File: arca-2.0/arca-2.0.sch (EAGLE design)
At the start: 192 parts, among them IC1 MCP6N11R, IC2 MCP6N11R, IC3 MCP6N11R, IC4 MCP6N11R, IC5 LM324D, IC6 LM324D, SW1 1101M2S3CQE2, SW2 1101M2S3CQE2, T1 FQP30N06L, T2 FQP30N06L, T3 FQP30N06L, T4 FQP30N06L, T5 FQP30N06L, T6 FQP30N06L, X1 2540-5

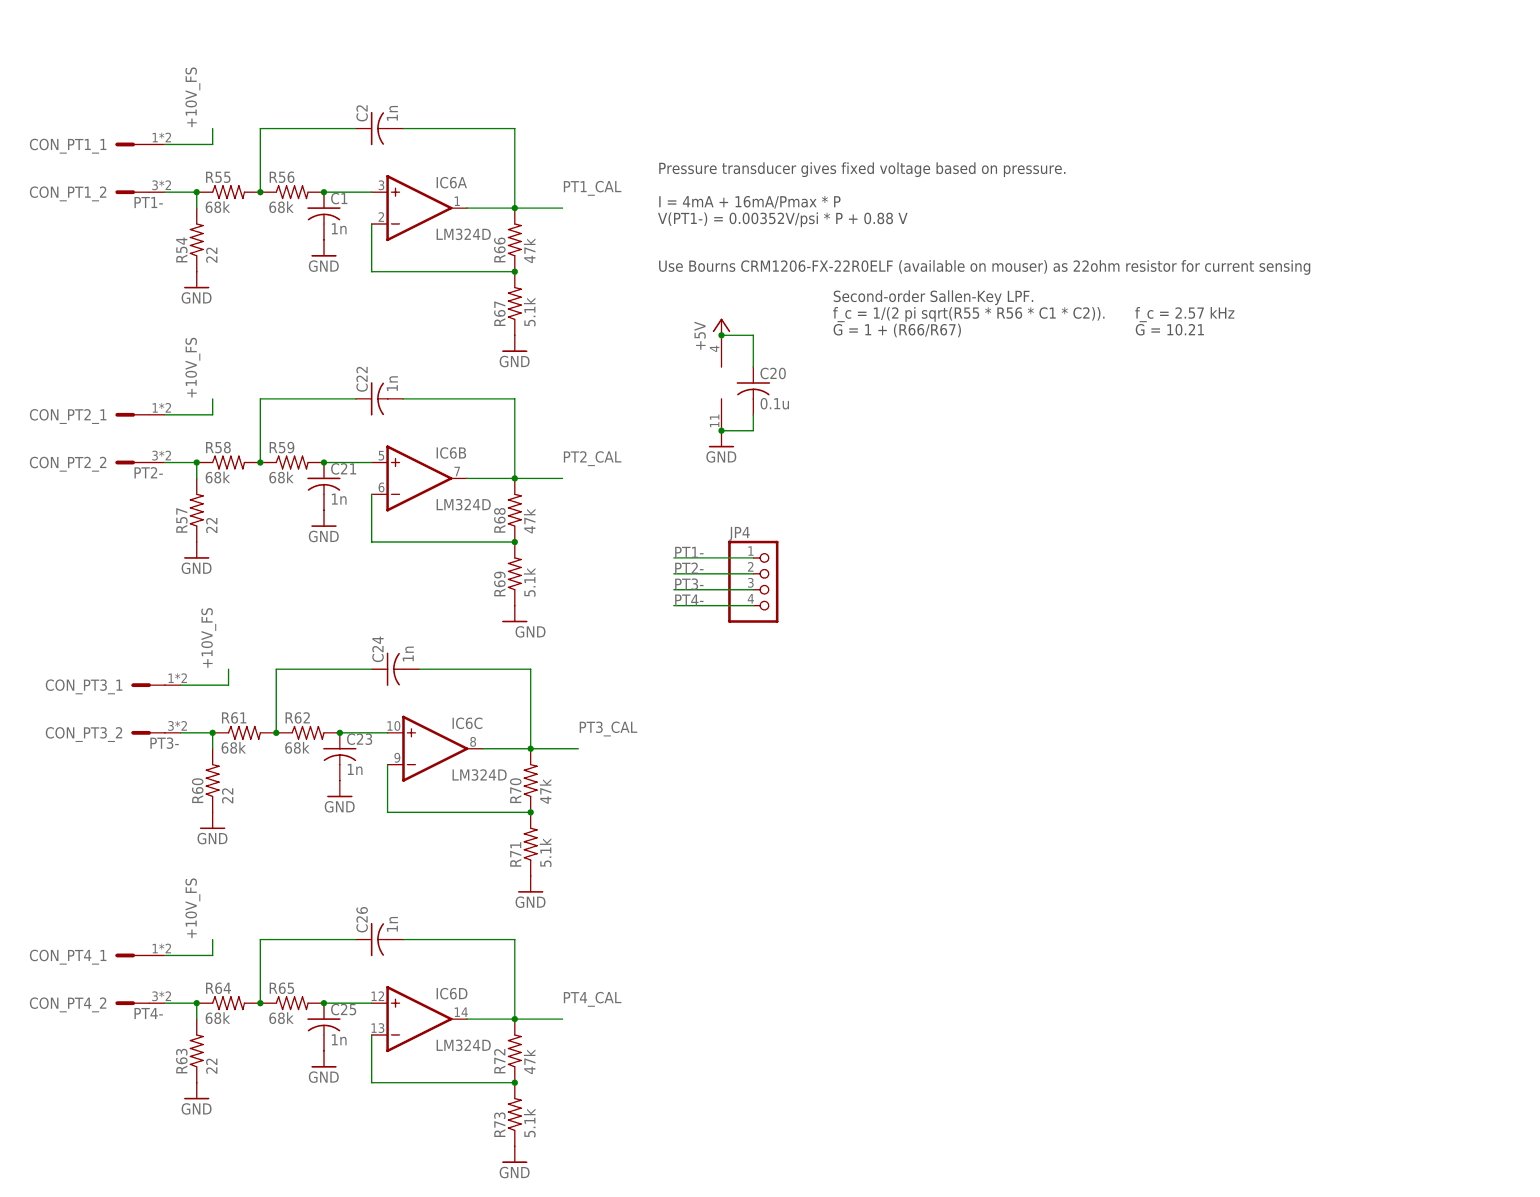
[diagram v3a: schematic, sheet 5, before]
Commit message: separate fuses for each external connection + LM324s on +10V
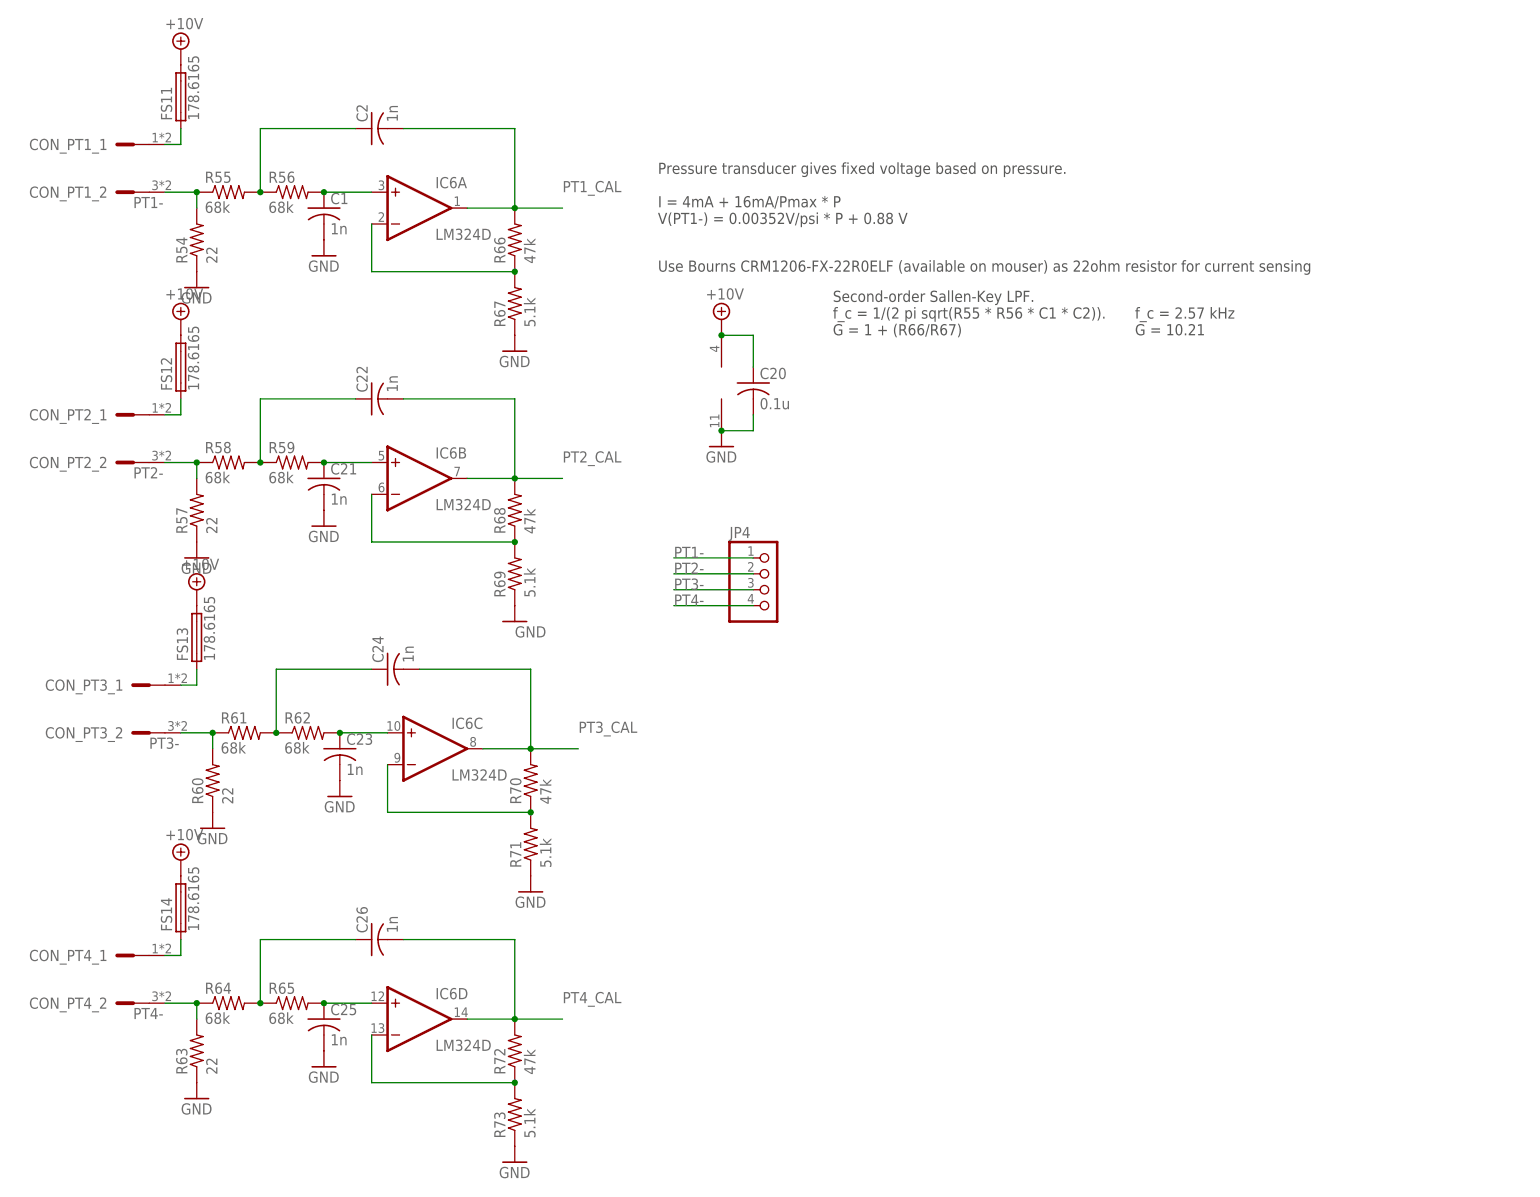
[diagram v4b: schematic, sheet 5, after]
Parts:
- added FS10, FS11, FS12, FS13, FS14, FS15, FS16, FS17, FS18, FS9: 178.6165, fuse-holder-littlefuse:178.6165
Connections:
- removed net +10V_FS: CON_PT1_1.SK, CON_PT2_1.SK, CON_PT3_1.SK, CON_PT4_1.SK, FS7.1
- removed net +5V_FS: CON_LC1_1.SK, CON_LC2_1.SK, CON_LC3_1.SK, CON_LC4_1.SK, CON_TC1_1.SK, CON_TC2_1.SK, CON_TC3_1.SK, CON_TC4_1.SK, FS8.1
- new net N$61: CON_LC1_1.SK, FS7.1
- new net N$62: CON_LC2_1.SK, FS8.1
- new net N$63: CON_LC3_1.SK, FS9.1
- new net N$64: CON_LC4_1.SK, FS10.1
- new net N$65: CON_PT1_1.SK, FS11.1
- new net N$66: CON_PT2_1.SK, FS12.1
- new net N$69: CON_PT3_1.SK, FS13.1
- new net N$70: CON_PT4_1.SK, FS14.1
- new net N$71: CON_TC1_1.SK, FS15.1
- new net N$72: CON_TC2_1.SK, FS16.1
- new net N$73: CON_TC3_1.SK, FS17.1
- new net N$74: CON_TC4_1.SK, FS18.1
- net +10V: now also C11.1, C20.1, FS11.2, FS12.2, FS13.2, FS14.2, IC5P.V+, IC6P.V+; no longer FS7.2
- net +5V: now also FS10.2, FS15.2, FS16.2, FS17.2, FS18.2, FS7.2, FS9.2; no longer C11.1, C20.1, IC5P.V+, IC6P.V+

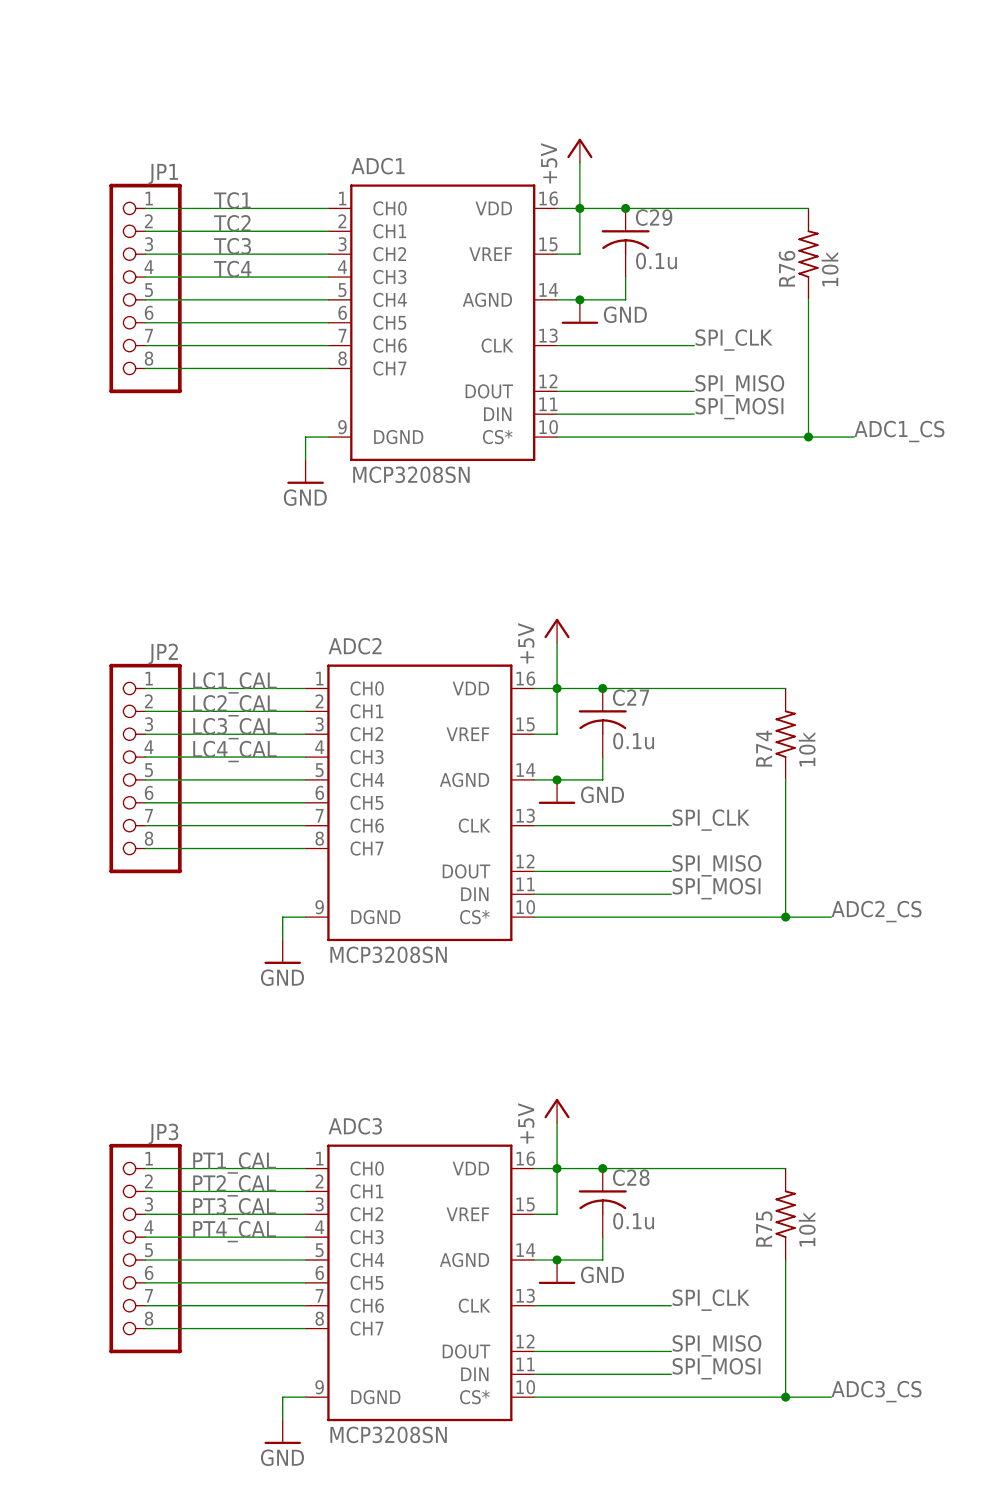
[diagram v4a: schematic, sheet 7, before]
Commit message: laying out extra breakers in board
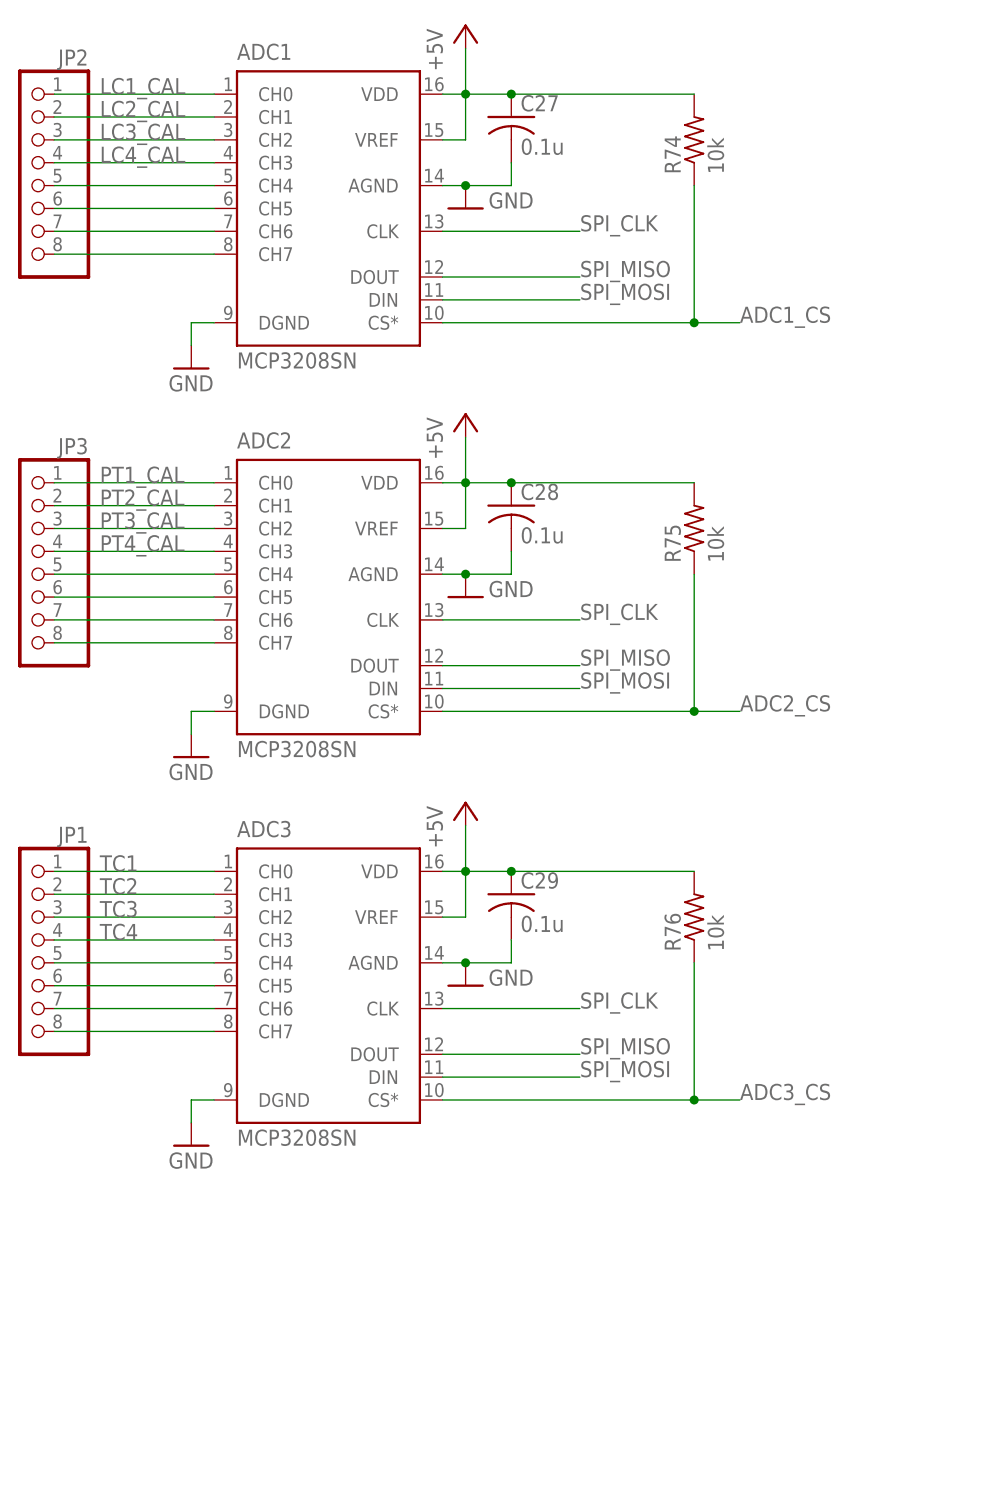
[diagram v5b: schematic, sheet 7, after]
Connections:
- net ADC1_CS: now also R74.1, X1-22.KL; no longer R76.1, X1-26.KL
- net ADC2_CS: now also R75.1; no longer R74.1
- net ADC3_CS: now also R76.1, X1-26.KL; no longer R75.1, X1-22.KL
- net LC1_CAL: now also ADC1.CH0; no longer ADC2.CH0
- net LC2_CAL: now also ADC1.CH1; no longer ADC2.CH1
- net LC3_CAL: now also ADC1.CH2; no longer ADC2.CH2
- net LC4_CAL: now also ADC1.CH3; no longer ADC2.CH3
- net N$49: now also ADC3.CH4; no longer ADC1.CH4
- net N$50: now also ADC3.CH5; no longer ADC1.CH5
- net N$51: now also ADC3.CH6; no longer ADC1.CH6
- net N$52: now also ADC3.CH7; no longer ADC1.CH7
- net N$53: now also ADC1.CH7; no longer ADC2.CH7
- net N$54: now also ADC1.CH6; no longer ADC2.CH6
- net N$55: now also ADC1.CH5; no longer ADC2.CH5
- net N$56: now also ADC1.CH4; no longer ADC2.CH4
- net N$57: now also ADC2.CH4; no longer ADC3.CH4
- net N$58: now also ADC2.CH5; no longer ADC3.CH5
- net N$59: now also ADC2.CH6; no longer ADC3.CH6
- net N$60: now also ADC2.CH7; no longer ADC3.CH7
- net PT1_CAL: now also ADC2.CH0; no longer ADC3.CH0
- net PT2_CAL: now also ADC2.CH1; no longer ADC3.CH1
- net PT3_CAL: now also ADC2.CH2; no longer ADC3.CH2
- net PT4_CAL: now also ADC2.CH3; no longer ADC3.CH3
- net TC1: now also ADC3.CH0; no longer ADC1.CH0
- net TC2: now also ADC3.CH1; no longer ADC1.CH1
- net TC3: now also ADC3.CH2; no longer ADC1.CH2
- net TC4: now also ADC3.CH3; no longer ADC1.CH3
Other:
- moved on the sheet: ADC1, ADC2, ADC3, C27, C28, C29, JP1, JP2, JP3, R74, R75, R76

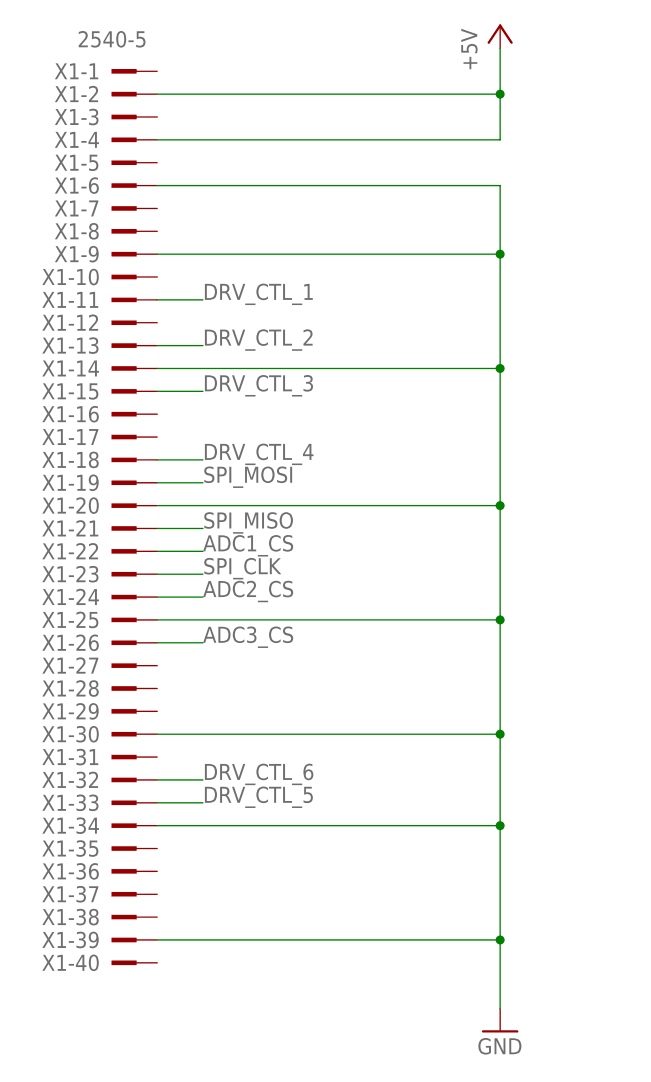
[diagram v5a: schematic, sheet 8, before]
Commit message: heartbeat light
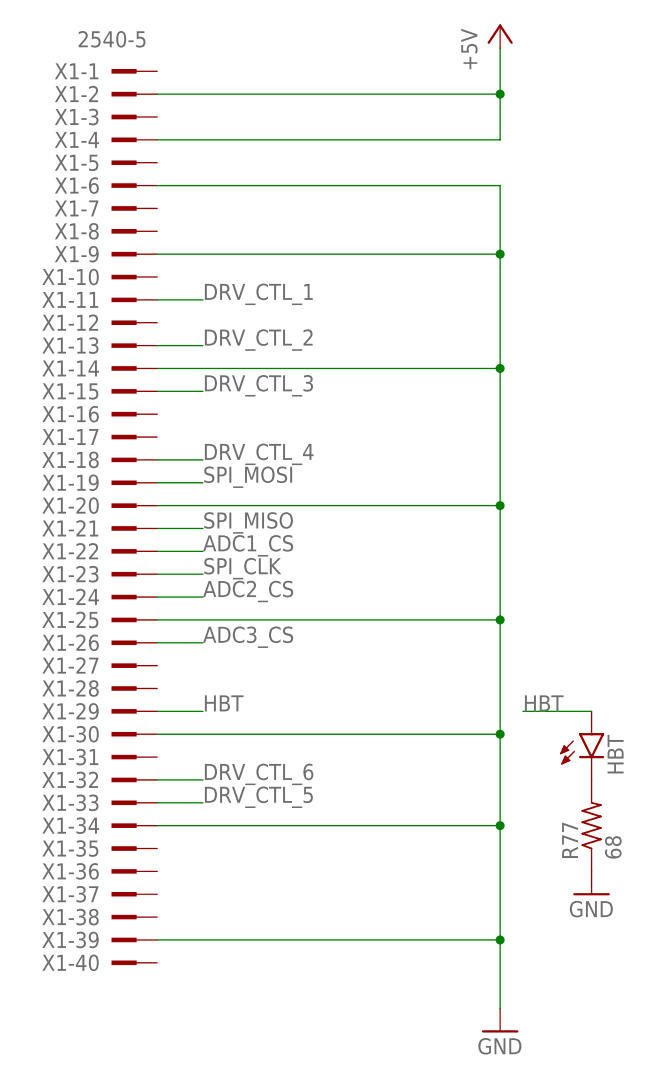
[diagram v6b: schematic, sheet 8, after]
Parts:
- added HBT: (no value), led:LEDCHIPLED_1206
- added R77: 68, rcl:R-US_R1206
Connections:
- new net HBT: HBT.A, X1-29.KL
- new net N$75: HBT.C, R77.2
- net GND: now also R77.1
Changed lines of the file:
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@@
 <part name="P+33" library="supply1" library_urn="urn:adsk.eagle:library:371" deviceset="+5V" device=""/>
 <part name="P+34" library="supply1" library_urn="urn:adsk.eagle:library:371" deviceset="+5V" device=""/>
+<part name="HBT" library="led" library_urn="urn:adsk.eagle:library:259" deviceset="LED" device="CHIPLED_1206" package3d_urn="urn:adsk.eagle:package:15823/2"/>
+<part name="R77" library="rcl" library_urn="urn:adsk.eagle:library:334" deviceset="R-US_" device="R1206" package3d_urn="urn:adsk.eagle:package:23540/2" value="68"/>
+<part name="GND69" library="supply1" library_urn="urn:adsk.eagle:library:371" deviceset="GND" device=""/>
 </parts>
 <sheets>
@@
 <attribute name="VALUE" x="86.36" y="40.64" size="1.778" layer="96"/>
 </instance>
+<instance part="HBT" gate="G$1" x="99.06" y="76.2" smashed="yes">
+<attribute name="NAME" x="102.616" y="71.628" size="1.778" layer="95" rot="R90"/>
+<attribute name="VALUE" x="104.775" y="71.628" size="1.778" layer="96" rot="R90"/>
+</instance>
+<instance part="R77" gate="G$1" x="99.06" y="66.04" smashed="yes" rot="R90">
+<attribute name="NAME" x="97.5614" y="62.23" size="1.778" layer="95" rot="R90"/>
+<attribute name="VALUE" x="102.362" y="62.23" size="1.778" layer="96" rot="R90"/>
+</instance>
+<instance part="GND69" gate="1" x="99.06" y="58.42" smashed="yes">
+<attribute name="VALUE" x="96.52" y="55.88" size="1.778" layer="96"/>
+</instance>
 </instances>
 <busses>
@@
 <junction x="88.9" y="129.54"/>
 </segment>
+<segment>
+<pinref part="R77" gate="G$1" pin="1"/>
+<pinref part="GND69" gate="1" pin="GND"/>
+</segment>
 </net>
 <net name="SPI_CLK" class="0">
@@
 </segment>
 </net>
+<net name="HBT" class="0">
+<segment>
+<pinref part="X1" gate="-29" pin="KL"/>
+<wire x1="50.8" y1="78.74" x2="55.88" y2="78.74" width="0.1524" layer="91"/>
+<label x="55.88" y="78.74" size="1.778" layer="95"/>
+</segment>
+<segment>
+<pinref part="HBT" gate="G$1" pin="A"/>
+<wire x1="99.06" y1="78.74" x2="91.44" y2="78.74" width="0.1524" layer="91"/>
+<label x="91.44" y="78.74" size="1.778" layer="95"/>
+</segment>
+</net>
+<net name="N$75" class="0">
+<segment>
+<pinref part="HBT" gate="G$1" pin="C"/>
+<pinref part="R77" gate="G$1" pin="2"/>
+</segment>
+</net>
